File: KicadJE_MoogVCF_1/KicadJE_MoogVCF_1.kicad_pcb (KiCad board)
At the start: 2 copper layers, 100 x 100 mm, 100 parts, among them J201 CV2, J202 Input2, J203 CV1, J204 Out VCF, J205 Input1, P201 Doepfer_Power_10pin, Q201 UMX1N, Q202 SS9014, Q203 SS9014, Q204 SS9014, Q205 SS9014, Q206 SS9014, Q207 SS9014, Q208 UMX1N, Q209 UMX1N, Q210 UMX1N, Q211 SS9014, Q212 SS9015, U201 TL072

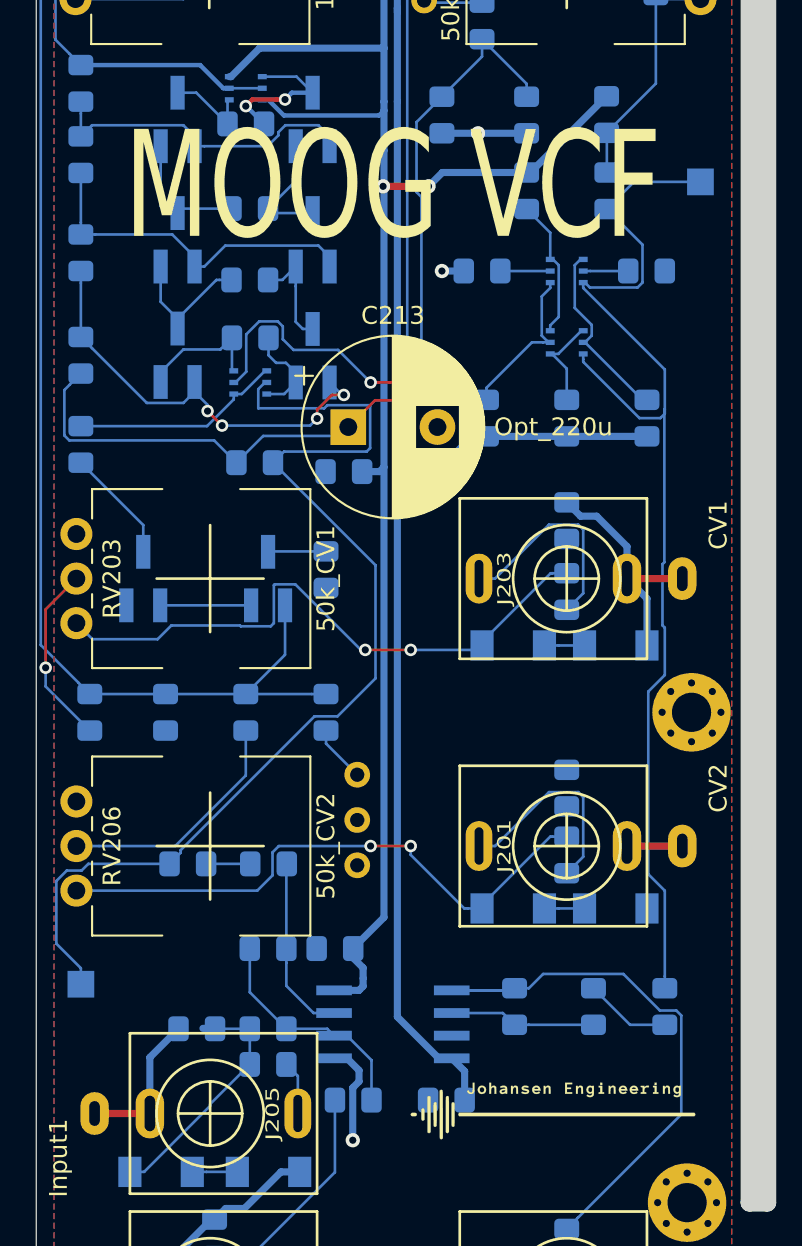
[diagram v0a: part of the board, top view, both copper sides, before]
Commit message: Trim added to PCB
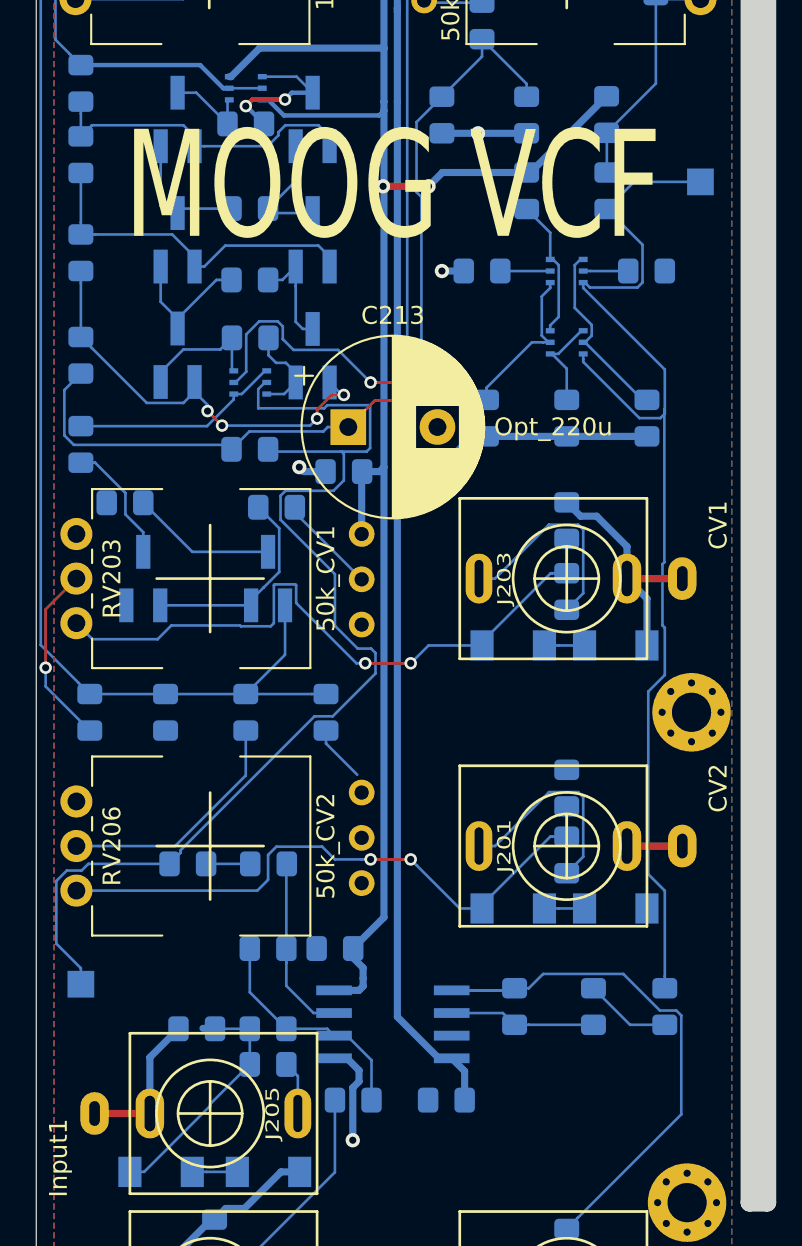
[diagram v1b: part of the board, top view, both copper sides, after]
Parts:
- removed G***: LOGO, AJ:Johansen_engineering_logo_20mm
- added R243: 100k, Resistor_SMD:R_0805_2012Metric_Pad1.15x1.40mm_HandSolder, B.Cu at (63.5, 101.0)
- added RV207: 10k, AJ-Dropbox-Kicad:Bourns3296WV, B.Cu at (68.2, 102.5)
- moved R239 11.9 mm to (55.0, 100.8), turned to 0 degrees
- moved RV205 1.03 mm to (68.2, 117.0)
- moved R225 0.80 mm to (62.0, 97.8)
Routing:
- net /KicadJE_Yousynth_MoogVCF/PNP_E: track 5.10 -> 11.7 mm
- net Net-(R243-Pad2): track 0.00 -> 5.59 mm
- net Net-(Q212-Pad3): track 3.26 -> 8.17 mm
- net Net-(C212-Pad1): track 59.8 -> 63.6 mm
- net +12V: track 135.0 -> 138.5 mm
- net GND: track 87.9 -> 89.5 mm, vias 3 -> 4
- net CV1: track 35.8 -> 37.0 mm

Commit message: DRC
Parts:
- moved R229 0.50 mm to (75.5, 73.7)
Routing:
- net Net-(R237-Pad1): track 3.20 -> 4.30 mm
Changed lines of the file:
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@@
     (thickness 1.6)
     (drawings 42)
-    (tracks 551)
+    (tracks 553)
     (zones 0)
     (modules 101)
@@
   )
   (module Resistor_SMD:R_0805_2012Metric_Pad1.15x1.40mm_HandSolder (layer B.Cu)
-    (at 75 73.725 90)
+    (at 75.5 73.725 90)
     (descr "Resistor SMD 0805 (2012 Metric), square (rectangular) end terminal, IPC_7351 nominal with elongated pad for handsoldering. (Body size source: https://docs.google.com/spreadsheets/d/1BsfQQcO9C6DZCsRaXUlFlo91Tg2WpOkGARC1WS5S8t0/edit?usp=sharing), generated with kicad-footprint-generator")
     (tags "resistor handsolder")
@@
   (segment (start 66.25 114.25) (end 66.25 113.525) (width 0.15) (layer B.Cu) (net 52) (status 20))
   (segment (start 68 116) (end 66.25 114.25) (width 0.15) (layer B.Cu) (net 52) (status 10))
+  (segment (start 68 116.75) (end 68.25 117) (width 0.15) (layer B.Cu) (net 52))
+  (segment (start 68 116) (end 68 116.75) (width 0.15) (layer B.Cu) (net 52))
   (via (at 50.525 110) (size 0.7) (drill 0.4) (layers F.Cu B.Cu) (net 53))
   (segment (start 52.25 105) (end 50.525 106.725) (width 0.15) (layer F.Cu) (net 53) (status 10))

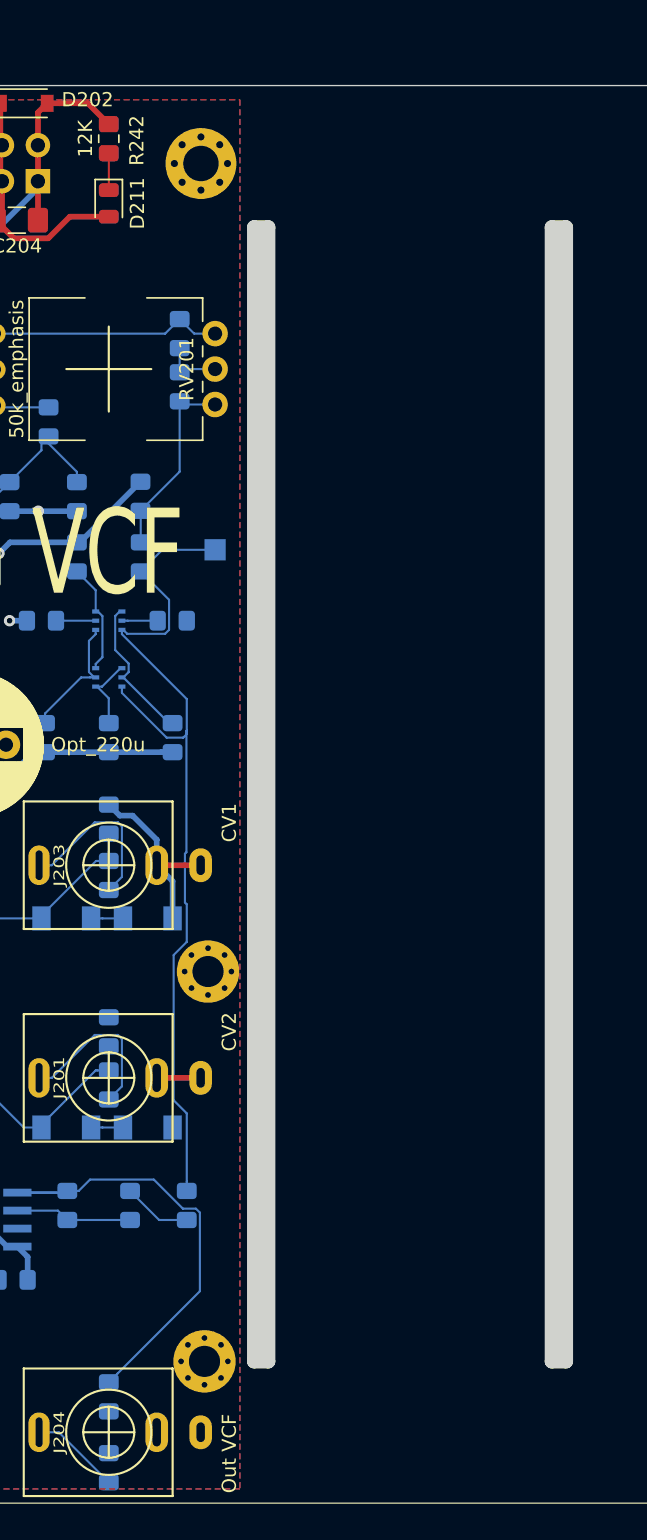
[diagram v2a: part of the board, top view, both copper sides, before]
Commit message: ADSR Routed
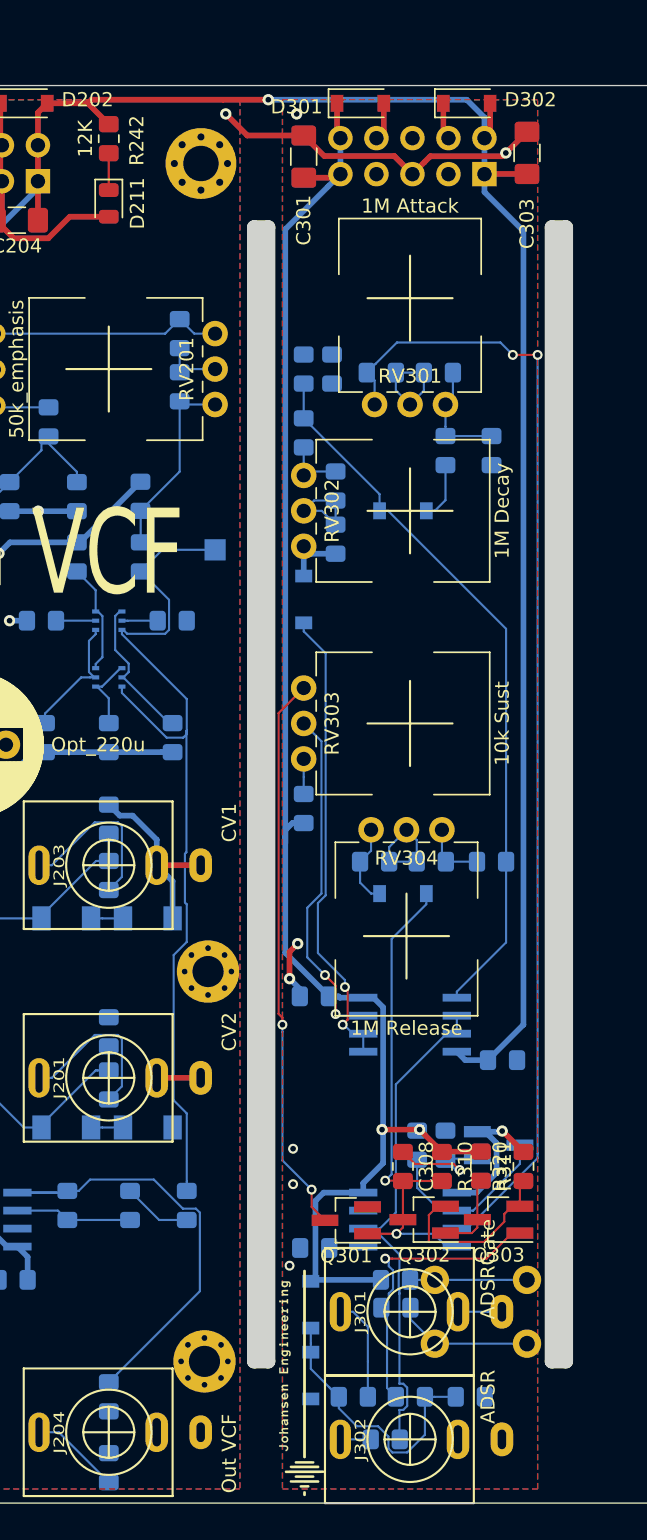
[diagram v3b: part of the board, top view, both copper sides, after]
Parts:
- added C301: 1u, Capacitor_SMD:C_1206_3216Metric_Pad1.42x1.75mm_HandSolder, F.Cu at (93.5, 55.0)
- added C302: 100n, Capacitor_SMD:C_0805_2012Metric_Pad1.15x1.40mm_HandSolder, B.Cu at (94.2, 114.2)
- added C303: 1u, Capacitor_SMD:C_1206_3216Metric_Pad1.42x1.75mm_HandSolder, F.Cu at (109.2, 54.8)
- added C304: 100n, Capacitor_SMD:C_0805_2012Metric_Pad1.15x1.40mm_HandSolder, B.Cu at (107.5, 118.8)
- added C305: 10n, Capacitor_SMD:C_0805_2012Metric_Pad1.15x1.40mm_HandSolder, B.Cu at (94.3, 132.0)
- added C306: 10u_N/A, Capacitor_SMD:C_0805_2012Metric_Pad1.15x1.40mm_HandSolder, B.Cu at (95.5, 70.0)
- added C307: 1u, Capacitor_SMD:C_0805_2012Metric_Pad1.15x1.40mm_HandSolder, B.Cu at (93.5, 70.0)
- added C308: 10n, Capacitor_SMD:C_0805_2012Metric_Pad1.15x1.40mm_HandSolder, F.Cu at (100.5, 126.2)
- added D301: 1N1007, Diode_SMD:D_SOD-123, F.Cu at (97.5, 51.2)
- added D302: 1N1007, Diode_SMD:D_SOD-123, F.Cu at (105.0, 51.2)
- added D303: 1N4148, Diode_SMD:D_SOD-123, B.Cu at (100.5, 80.0)
- added D304: 1N4148, Diode_SMD:D_SOD-123, B.Cu at (93.5, 86.2)
- added D305: 1N4148, Diode_SMD:D_SOD-123, B.Cu at (100.5, 107.0)
- added D306: 1N1007, Diode_SMD:D_SOD-123, B.Cu at (94.0, 136.0)
- added D307: 1N1007, Diode_SMD:D_SOD-123, B.Cu at (94.0, 141.0)
- added J301: ADSRGate, AJ-Dropbox-Kicad:PJ301SM, F.Cu at (101.0, 136.5)
- added J302: ADSR, AJ-Dropbox-Kicad:PJ301SM, F.Cu at (101.0, 145.5)
- added P301: Doepfer_Power_10pin, Connectors_IDC:IDC-Header_2x05_Pitch2.54mm_Straight, B.Cu at (106.2, 56.2)
- added Q301: SI2302, Package_TO_SOT_SMD:SOT-23_Handsoldering, F.Cu at (96.5, 130.1)
- added Q302: MMBT3904, Package_TO_SOT_SMD:SOT-23_Handsoldering, F.Cu at (102.0, 130.0)
- added Q303: MMBT3904, Package_TO_SOT_SMD:SOT-23_Handsoldering, F.Cu at (107.2, 130.0)
- added Q304: MMBT3904, Package_TO_SOT_SMD:SOT-23_Handsoldering, B.Cu at (107.2, 124.8)
- added R301: 0R, Resistor_SMD:R_0805_2012Metric_Pad1.15x1.40mm_HandSolder, B.Cu at (103.0, 70.2)
- added R302: Open, Resistor_SMD:R_0805_2012Metric_Pad1.15x1.40mm_HandSolder, B.Cu at (99.0, 70.2)
- added R303: 680R, Resistor_SMD:R_0805_2012Metric_Pad1.15x1.40mm_HandSolder, B.Cu at (103.5, 75.8)
- added R304: 120R_N/A, Resistor_SMD:R_0805_2012Metric_Pad1.15x1.40mm_HandSolder, B.Cu at (106.8, 75.8)
- added R305: 4k7, Resistor_SMD:R_0805_2012Metric_Pad1.15x1.40mm_HandSolder, B.Cu at (93.5, 101.0)
- added R306: 0R, Resistor_SMD:R_0805_2012Metric_Pad1.15x1.40mm_HandSolder, B.Cu at (95.8, 82.0)
- added R307: Open, Resistor_SMD:R_0805_2012Metric_Pad1.15x1.40mm_HandSolder, B.Cu at (95.8, 78.2)
- added R308: 100R, Resistor_SMD:R_0805_2012Metric_Pad1.15x1.40mm_HandSolder, B.Cu at (93.5, 74.5)
- added R309: 10k, Resistor_SMD:R_0805_2012Metric_Pad1.15x1.40mm_HandSolder, B.Cu at (100.0, 134.2)
- added R310: 22k, Resistor_SMD:R_0805_2012Metric_Pad1.15x1.40mm_HandSolder, F.Cu at (103.2, 126.2)
- added R311: 22k, Resistor_SMD:R_0805_2012Metric_Pad1.15x1.40mm_HandSolder, F.Cu at (106.0, 126.2)
- added R312: 22k, Resistor_SMD:R_0805_2012Metric_Pad1.15x1.40mm_HandSolder, B.Cu at (101.5, 124.8)
- added R313: 47k, Resistor_SMD:R_0805_2012Metric_Pad1.15x1.40mm_HandSolder, B.Cu at (100.0, 136.2)
- added R314: 1M, Resistor_SMD:R_0805_2012Metric_Pad1.15x1.40mm_HandSolder, B.Cu at (101.0, 142.5)
- added R315: 0R, Resistor_SMD:R_0805_2012Metric_Pad1.15x1.40mm_HandSolder, B.Cu at (98.5, 104.8)
- added R316: Open, Resistor_SMD:R_0805_2012Metric_Pad1.15x1.40mm_HandSolder, B.Cu at (102.5, 104.8)
- added R317: 1M2, Resistor_SMD:R_0805_2012Metric_Pad1.15x1.40mm_HandSolder, B.Cu at (105.2, 142.5)
- added R318: 1k, Resistor_SMD:R_0805_2012Metric_Pad1.15x1.40mm_HandSolder, B.Cu at (99.2, 145.5)
- added R319: 100R, Resistor_SMD:R_0805_2012Metric_Pad1.15x1.40mm_HandSolder, B.Cu at (106.8, 104.8)
- added R320: 10R, Resistor_SMD:R_0805_2012Metric_Pad1.15x1.40mm_HandSolder, F.Cu at (109.0, 126.2)
- added R321: 22k, Resistor_SMD:R_0805_2012Metric_Pad1.15x1.40mm_HandSolder, B.Cu at (103.5, 124.8)
- added R322: 47k, Resistor_SMD:R_0805_2012Metric_Pad1.15x1.40mm_HandSolder, B.Cu at (97.0, 142.5)
- added RV301: 1M Attack, AJ-Dropbox-Kicad:Potentiometer_China_RK09_Single_Vertical_AJ, F.Cu at (103.5, 72.5)
- added RV302: 1M Decay, AJ-Dropbox-Kicad:Potentiometer_China_RK09_Single_Vertical_AJ, F.Cu at (93.5, 82.5)
- added RV303: 10k Sust, Potentiometer_THT:Potentiometer_China_RK09_Single_Vertical_AJ, F.Cu at (93.5, 97.5)
- added RV304: 1M Release, AJ-Dropbox-Kicad:Potentiometer_China_RK09_Single_Vertical_AJ, F.Cu at (98.2, 102.5)
- added SW301: SW_DPDT_x2, AJ:Johansen_engineering_logo_20mm, F.Cu at (93.5, 141.5)
- added SW302: Gate, Button_Switch_THT:SW_PUSH_6mm, B.Cu at (102.8, 138.8)
- added U301: TL072, AJ-Dropbox-Kicad:AJ_SO-8_5.3x6.2mm_P1.27mm, B.Cu at (101.0, 116.2)
- added U302: TLC555, AJ-Dropbox-Kicad:AJ_SO-8_5.3x6.2mm_P1.27mm, B.Cu at (101.0, 130.0)
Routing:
- net +12V: track 138.5 -> 249.9 mm, vias 2 -> 4
- net -12V: track 110.0 -> 215.4 mm, vias 0 -> 1
- net 555_Out: track 0.00 -> 80.2 mm, vias 0 -> 2
- net Net-(C307-Pad2): track 0.00 -> 51.0 mm
- net GND: track 89.5 -> 134.3 mm, vias 4 -> 13
- net Net-(Q301-Pad3): track 0.00 -> 40.2 mm, vias 0 -> 2
- net 555_RST: track 0.00 -> 36.2 mm, vias 0 -> 2
- net 555_Threshold: track 0.00 -> 35.4 mm
- net Net-(D304-Pad1): track 0.00 -> 33.2 mm, vias 0 -> 2
- net Net-(RV303-Pad2): track 0.00 -> 24.3 mm, vias 0 -> 2
- net Net-(Q303-Pad1): track 0.00 -> 20.7 mm, vias 0 -> 1
- net ADSRGate: track 0.00 -> 20.6 mm
- net Net-(Q302-Pad2): track 0.00 -> 13.0 mm
- net 555_Trig: track 0.00 -> 12.6 mm
- net Net-(R313-Pad2): track 0.00 -> 9.75 mm
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
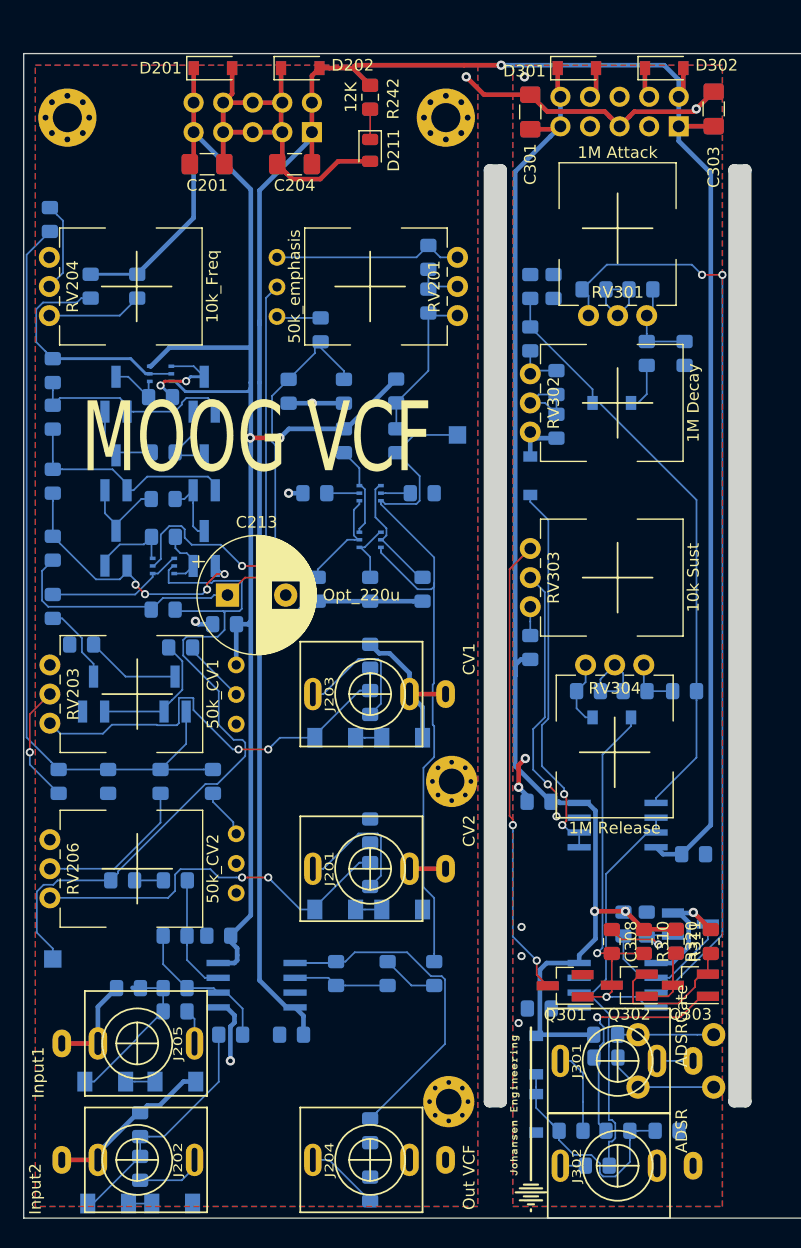
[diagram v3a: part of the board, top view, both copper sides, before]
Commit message: Labels ADSR
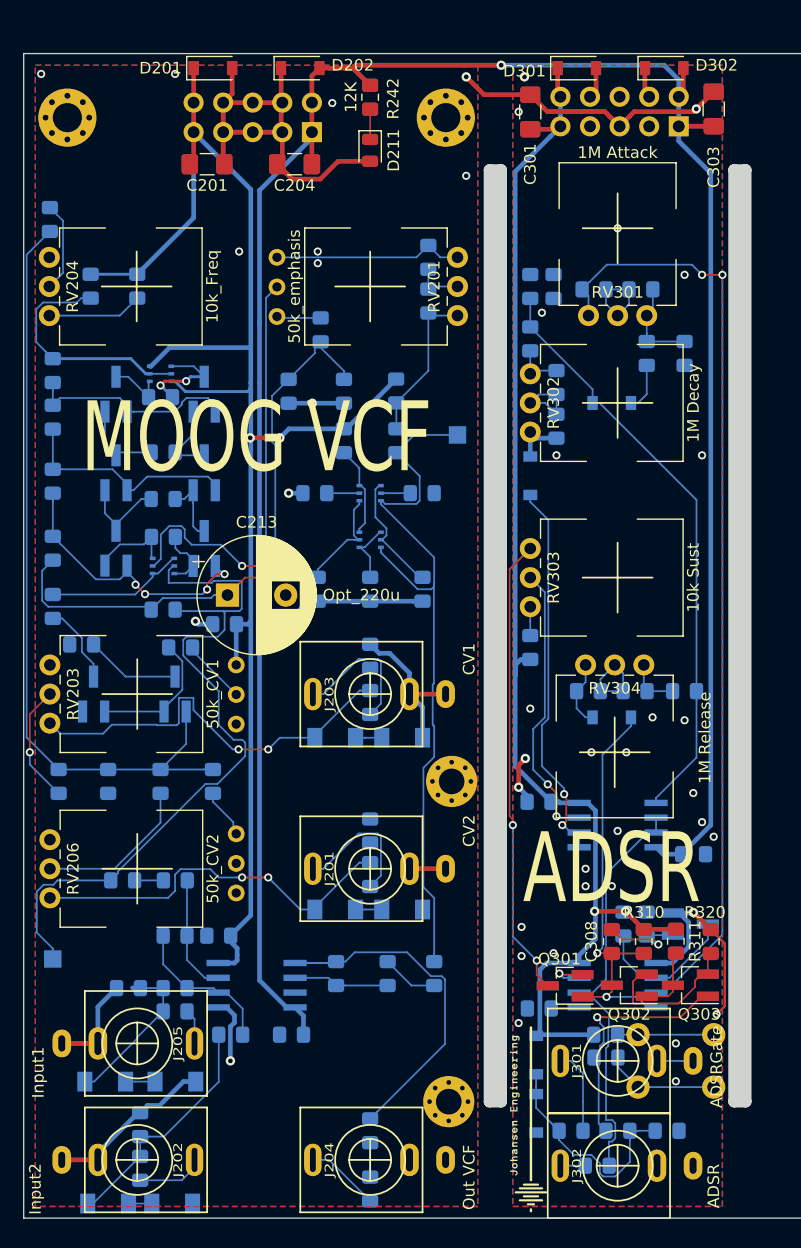
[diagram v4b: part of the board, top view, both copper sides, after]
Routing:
- net GND: track 134.3 -> 142.3 mm, vias 13 -> 42
- net 555_Dis: track 0.00 -> 3.89 mm, vias 0 -> 1
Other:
- board text added: "ADSR"
- board text added: "Yousynth ADSR Rev A - 07/10-2019 Johansen Engineering"
